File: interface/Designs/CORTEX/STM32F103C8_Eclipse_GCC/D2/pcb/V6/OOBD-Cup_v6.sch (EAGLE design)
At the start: 71 parts, among them IC1 24LC16, IC2 BTM-182, IC3 PCA82C250T, IC4 MC34063-SO, IC5 78L05SMD, Q1 8MHz, T1 BC817, T2 BC817, T3 BC817, T4 BC817, U1 STM32F10XTXU6

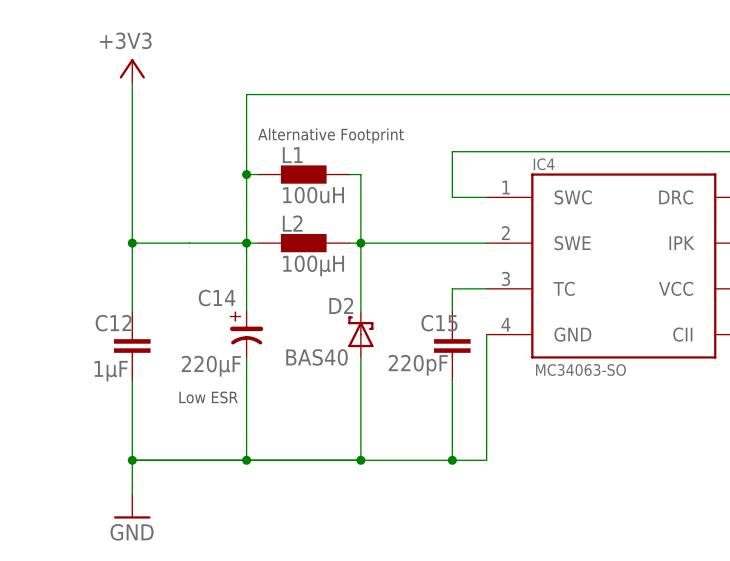
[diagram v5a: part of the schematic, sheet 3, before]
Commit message: add necessary modifications for switching regulator MC34063
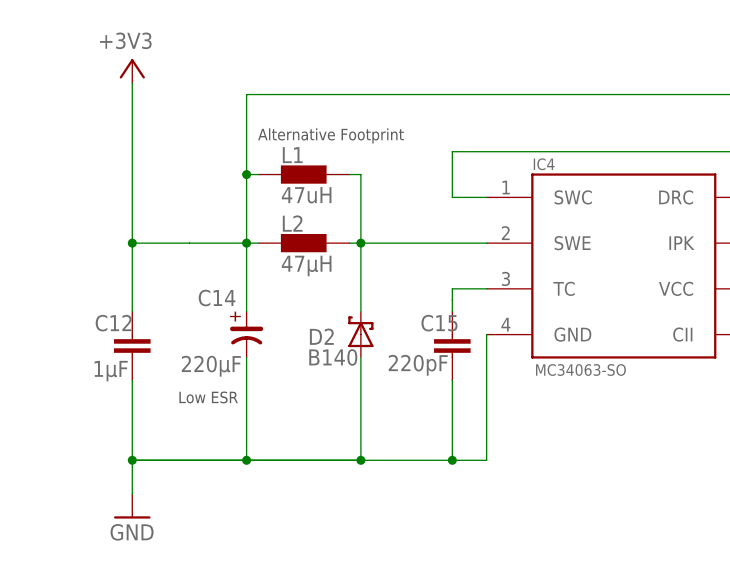
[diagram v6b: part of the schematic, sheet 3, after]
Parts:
- D2: value BAS40 -> B140; device diode:BAS40 -> diode:SCHOTTKY-DIODESMD
- L1: value 100uH -> 47uH
- L2: value 100µH -> 47µH
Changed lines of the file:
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@@
 <part name="R24" library="rcl" deviceset="R-EU_" device="R0805" value="1R"/>
 <part name="R21" library="rcl" deviceset="R-EU_" device="R0603" value="3k3"/>
-<part name="D2" library="diode" deviceset="BAS40" device=""/>
-<part name="L2" library="Inductor-Fastron" deviceset="07HCP-XXXX-50" device="" value="100µH"/>
+<part name="L2" library="Inductor-Fastron" deviceset="07HCP-XXXX-50" device="" value="47µH"/>
 <part name="GND14" library="supply1" deviceset="GND" device=""/>
 <part name="GND15" library="supply1" deviceset="GND" device=""/>
@@
 <part name="GND17" library="supply1" deviceset="GND" device=""/>
 <part name="+3V4" library="supply1" deviceset="+3V3" device=""/>
-<part name="L1" library="Inductor-Fastron" deviceset="PIS2408" device="" value="100uH"/>
+<part name="L1" library="Inductor-Fastron" deviceset="PIS2408" device="" value="47uH"/>
 <part name="R22" library="rcl" deviceset="R-EU_" device="R0805" value="1R"/>
 <part name="IC3" library="can" deviceset="PCA82C250" device="T"/>
@@
 <part name="R9" library="resistor" deviceset="R-EU_" device="R0603" value="4k7"/>
 <part name="+3V9" library="supply1" deviceset="+3V3" device=""/>
+<part name="D2" library="diode" deviceset="SCHOTTKY-DIODE" device="SMD" value="B140"/>
 </parts>
 <sheets>
@@
 <attribute name="VALUE" x="96.52" y="127.254" size="1.778" layer="96"/>
 </instance>
-<instance part="D2" gate="1" x="45.72" y="139.7" smashed="yes" rot="R90">
-<attribute name="NAME" x="45.085" y="143.764" size="1.778" layer="95" rot="R180"/>
-<attribute name="VALUE" x="37.211" y="136.271" size="1.778" layer="96"/>
-</instance>
 <instance part="L2" gate="G$1" x="39.37" y="149.86" smashed="yes">
 <attribute name="NAME" x="36.83" y="151.13" size="1.778" layer="95"/>
@@
 <instance part="GND27" gate="1" x="10.16" y="43.18"/>
 <instance part="GND28" gate="1" x="99.06" y="43.18"/>
+<instance part="D2" gate="G$1" x="45.72" y="139.7" smashed="yes" rot="R90">
+<attribute name="NAME" x="42.926" y="140.335" size="1.778" layer="95" rot="R180"/>
+<attribute name="VALUE" x="45.466" y="138.049" size="1.778" layer="96" rot="R180"/>
+</instance>
 </instances>
 <busses>
@@
 <junction x="20.32" y="125.73"/>
 <pinref part="GND14" gate="1" pin="GND"/>
-<pinref part="D2" gate="1" pin="A"/>
 <pinref part="C12" gate="G$1" pin="2"/>
 <pinref part="C15" gate="G$1" pin="2"/>
 <pinref part="IC4" gate="G$1" pin="GND"/>
 <pinref part="C14" gate="G$1" pin="-"/>
+<pinref part="D2" gate="G$1" pin="A"/>
 </segment>
 <segment>
@@
 <wire x1="45.72" y1="157.48" x2="45.72" y2="149.86" width="0.1524" layer="91"/>
 <junction x="45.72" y="149.86"/>
-<pinref part="D2" gate="1" pin="C"/>
 <pinref part="L2" gate="G$1" pin="P$2"/>
 <pinref part="IC4" gate="G$1" pin="SWE"/>
 <pinref part="L1" gate="G$1" pin="P$2"/>
-</segment>
-</net>
+<pinref part="D2" gate="G$1" pin="C"/>
+</segment>
+</net>

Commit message: add latest modification for optional WLAN-Interface
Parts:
- added JP3: (no value), jumper:JP1E
- JP1: device jumper:JP4Q -> jumper:JP5Q
- JP2: value (none) -> ext. WLAN; device jumper:JP1E -> jumper:JP3Q
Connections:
- removed net N$4: LED1.AR, R8.2
- removed net N$6: LED1.AG, R7.2
- removed net N$7: LED2.C, R15.1
- new net 3V3_BTM182: C5.1, C6.1, IC2.VDD, IC2.VDD_USB, JP1.9
- new net LED1_GR: JP2.1, LED1.AG, R7.2
- new net LED1_RT: JP2.3, LED1.AR, R8.2
- new net LED2_BL: JP2.4, LED2.C, R15.1
- net +12V: now also JP2.2
- net +3V3: now also JP1.10, JP1.8; no longer C5.1, C6.1, IC2.VDD, IC2.VDD_USB, JP1.1
- net BOOT0: now also JP1.7; no longer JP1.2
- net BTM_RX: now also JP1.1; no longer JP1.8
- net BTM_TX: now also JP1.3; no longer JP1.6
- net BUZZER: now also R13.1; no longer R14.1
- net GND: now also JP1.6, JP2.5; no longer JP1.3
- net LED_BLUE: now also R14.1; no longer R13.1
- net N$10: now also T3.C; no longer T2.C
- net N$16: now also JP3.2; no longer JP2.2
- net N$23: now also T2.C; no longer T3.C
- net N$3: now also JP3.1; no longer JP2.1
- net RESET-: now also JP1.5; no longer JP1.4
- net STM_RXD: now also JP1.4; no longer JP1.5
- net STM_TXD: now also JP1.2; no longer JP1.7
- net VBAT: now also JP2.6
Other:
- moved on the sheet: C1, C2, C3, C4, IC1, LED1, LED2, Q1, R1, R13, R14, R15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
